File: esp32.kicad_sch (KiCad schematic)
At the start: 1 part

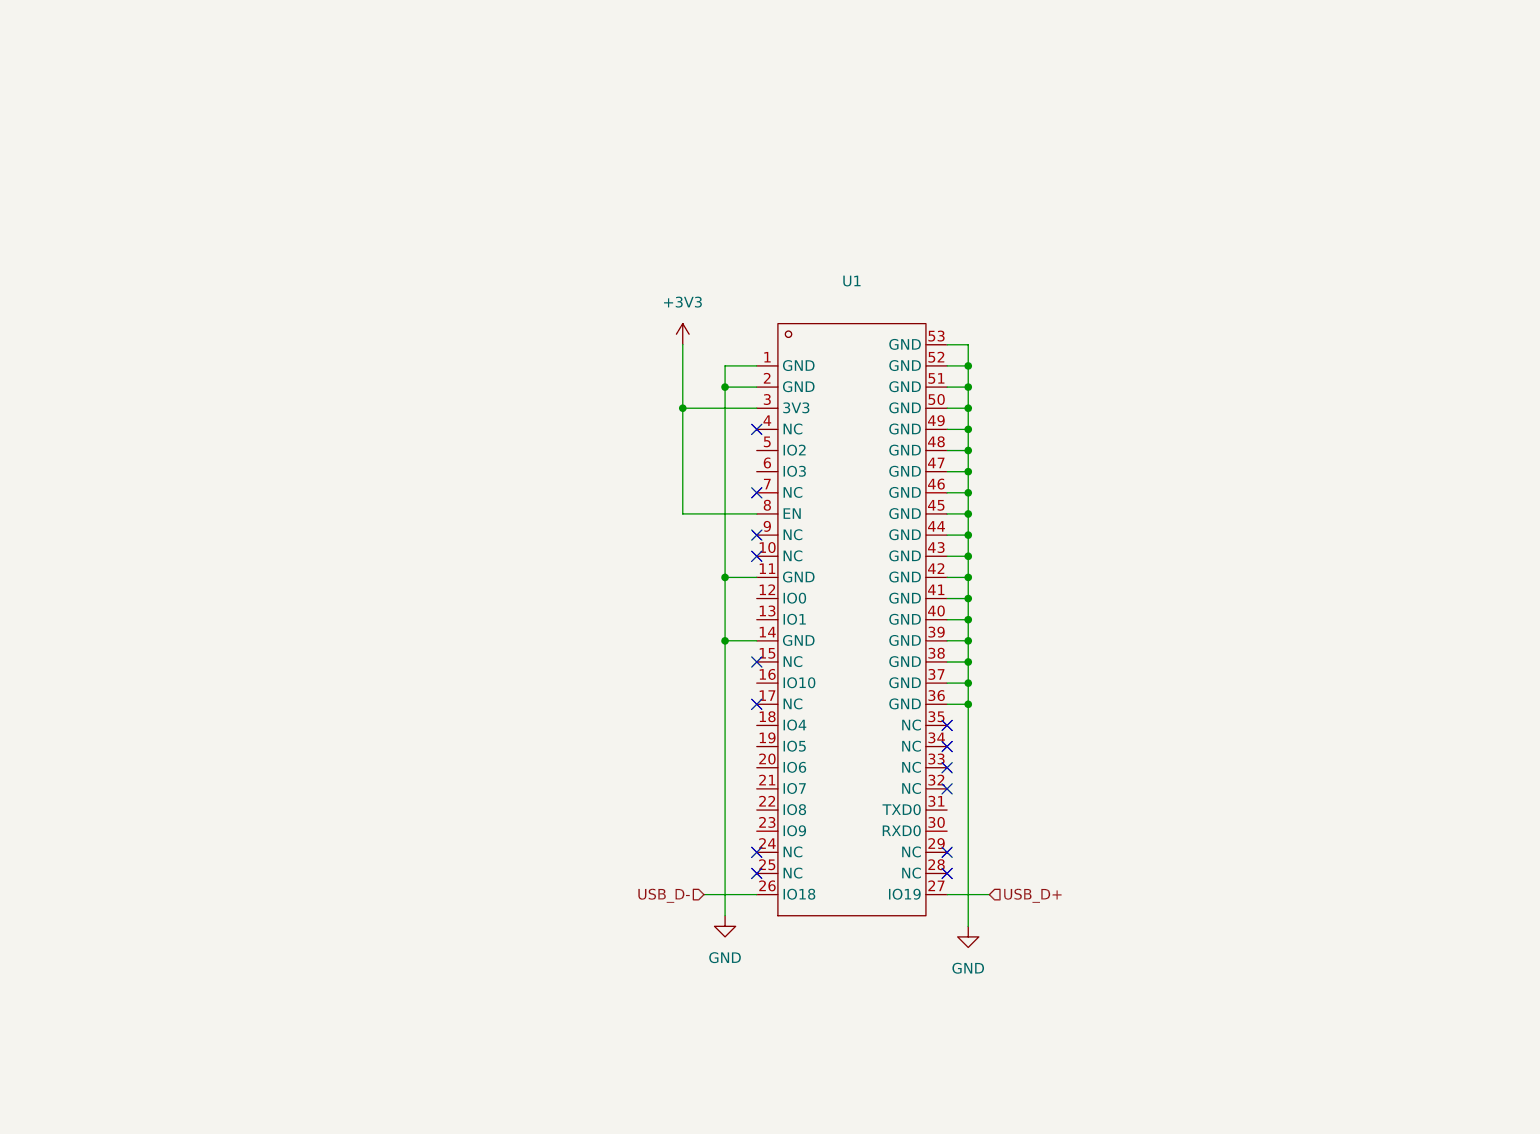
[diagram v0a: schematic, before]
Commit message: Finished the power, USB and ESP32 parts of the schematic
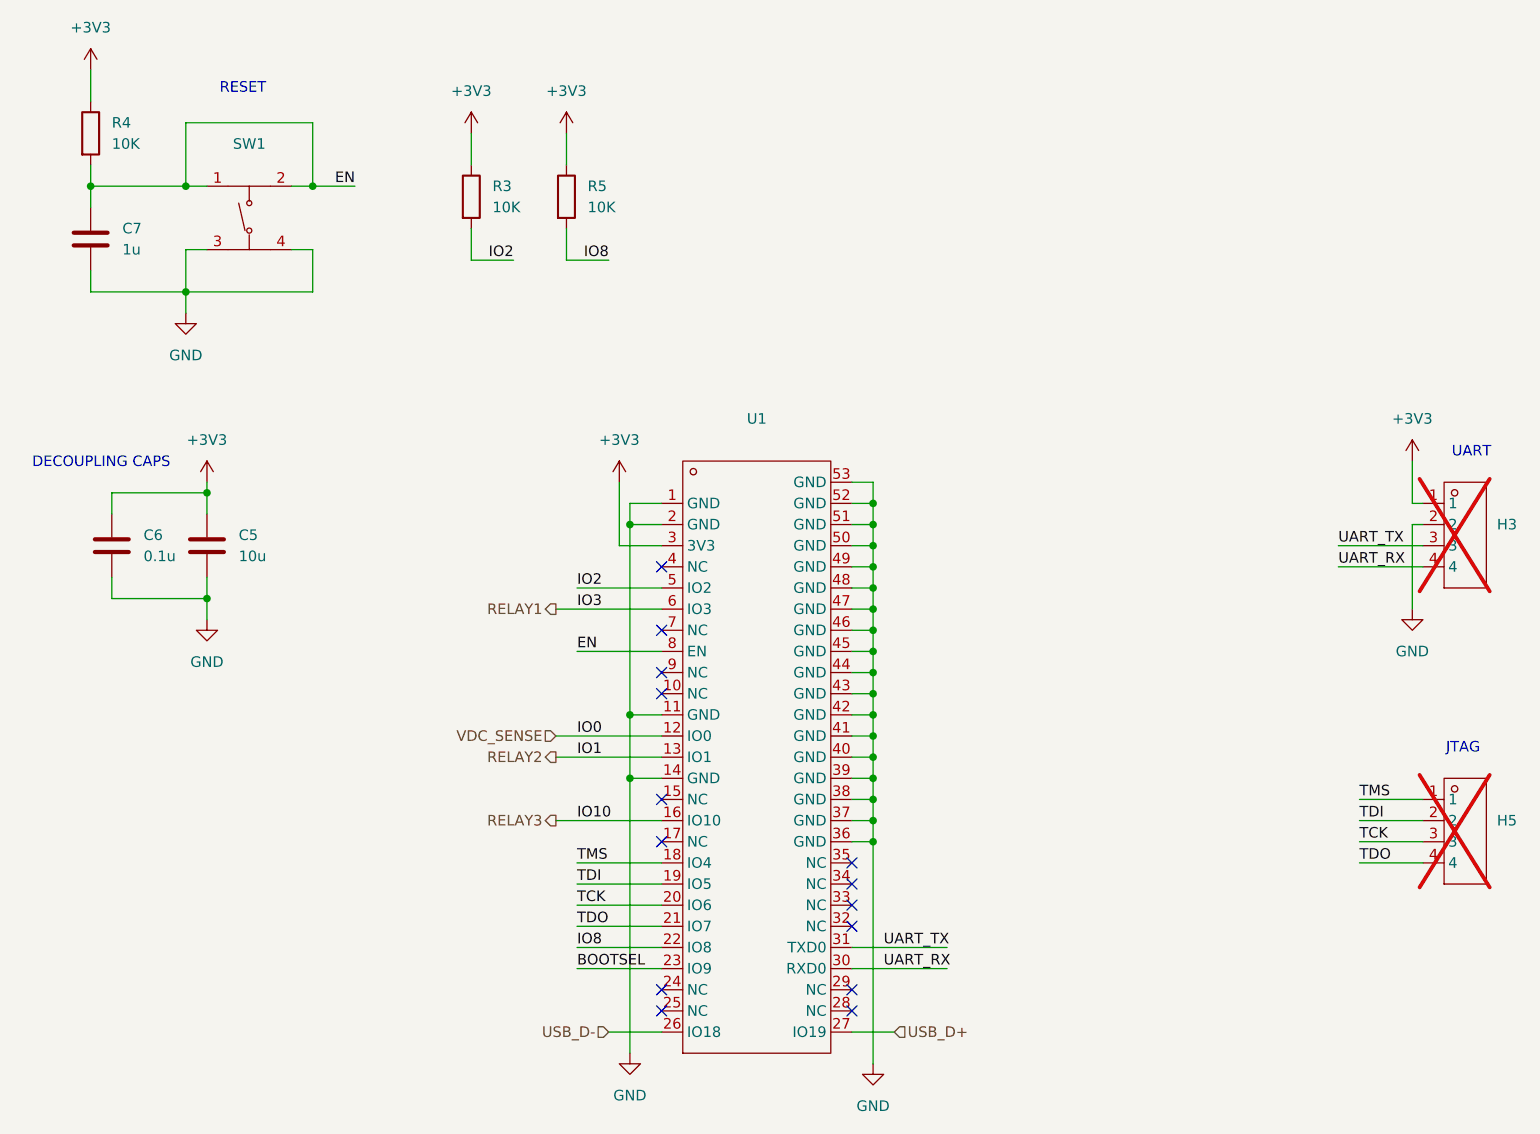
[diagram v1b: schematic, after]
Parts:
- added C5: 10u, Capacitor_SMD:C_0603_1608Metric, symbol Device:C
- added C6: 0.1u, Capacitor_SMD:C_0603_1608Metric, symbol Device:C
- added C7: 1u, Capacitor_SMD:C_0603_1608Metric, symbol Device:C
- added H3, H5: ~, EasyEDA_Lib:HDR-TH_4P-P2.54-V-M, symbol EasyEDA_Lib:PZ254V-11-04P_C2691448
- added R3, R4, R5: 10K, Resistor_SMD:R_0603_1608Metric, symbol Device:R
- added SW1: ~, EasyEDA_Lib:SW-SMD_4P-L4.2-W3.3-P2.15-LS5.1, symbol EasyEDA_Lib:TS-1089S-02526
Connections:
- net +3V3: now also C5.1, C6.1, H3.1, R3.1, R4.1, R5.1; no longer U1.8 (EN)
- net GND: now also C5.2, C6.2, C7.2, H3.2, SW1.3, SW1.4
- net VDC_SENSE: now reaches U1.12 (IO0)
- net RELAY2: now reaches U1.13 (IO1)
- net RELAY3: now reaches U1.16 (IO10)
- net TMS: now reaches U1.18 (IO4)
- net TMS: now also H5.1
- net TDI: now reaches U1.19 (IO5)
- net TDI: now also H5.2
- net TCK: now reaches U1.20 (IO6)
- net TCK: now also H5.3
- net TDO: now reaches U1.21 (IO7)
- net TDO: now also H5.4
- net IO8: now reaches U1.22 (IO8)
- net IO8: now also R5.2
- net BOOTSEL: now reaches U1.23 (IO9)
- net UART_RX: now reaches U1.30 (RXD0)
- net UART_RX: now also H3.4
- net UART_TX: now reaches U1.31 (TXD0)
- net UART_TX: now also H3.3
- net IO2: now reaches U1.5 (IO2)
- net IO2: now also R3.2
- net RELAY1: now reaches U1.6 (IO3)
- new net EN: C7.1, R4.2, SW1.1, SW1.2, U1.8 (EN)
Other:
- note added: "DECOUPLING CAPS"
- note added: "JTAG"
- note added: "RESET"
- note added: "UART"
- moved on the sheet: U1

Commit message: Finished schematics, started component placement
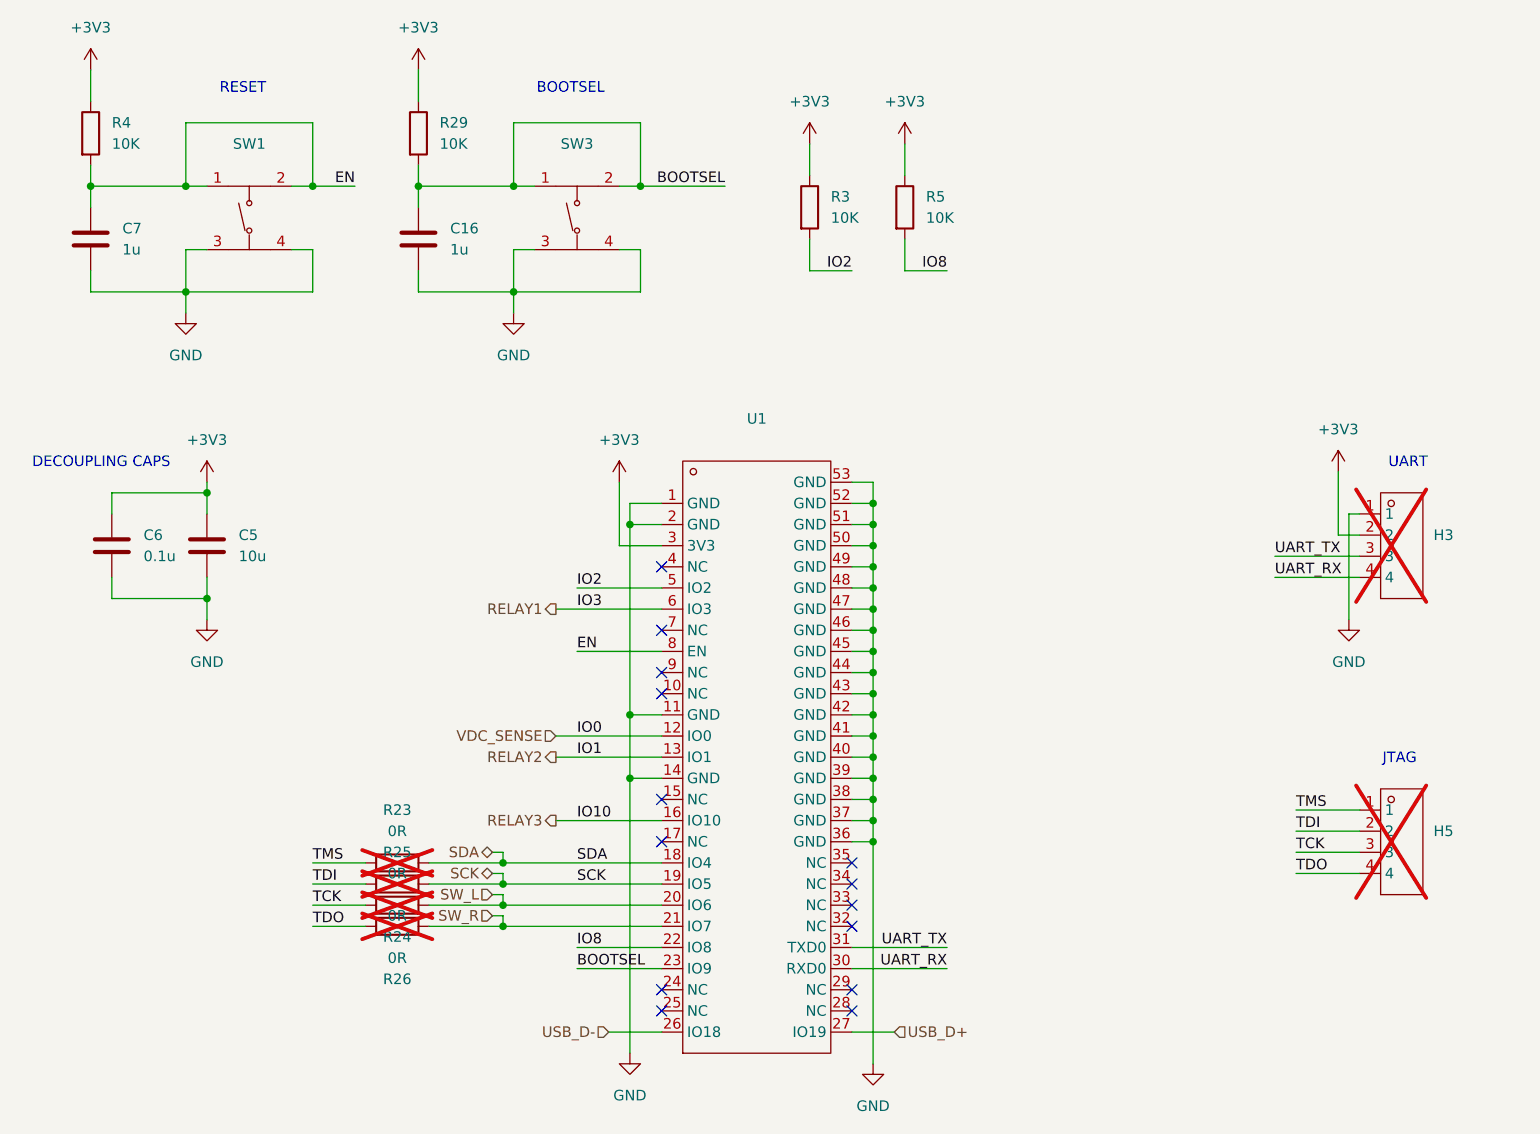
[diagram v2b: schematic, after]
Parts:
- added C16: 1u, Capacitor_SMD:C_0603_1608Metric, symbol Device:C
- added R23, R24, R25, R26: 0R, Resistor_SMD:R_0603_1608Metric, symbol Device:R
- added R29: 10K, Resistor_SMD:R_0603_1608Metric, symbol Device:R
- added SW3: ~, EasyEDA_Lib:SW-SMD_4P-L4.2-W3.3-P2.15-LS5.1, symbol EasyEDA_Lib:TS-1089S-02526
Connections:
- net +3V3: now also H3.2, R29.1; no longer H3.1
- net BOOTSEL: now also C16.1, R29.2, SW3.1, SW3.2
- net GND: now also H3.1, C16.2, SW3.3, SW3.4; no longer H3.2
- net TCK: now also R25.1; no longer U1.20 (IO6)
- net TDI: now also R24.1; no longer U1.19 (IO5)
- net TDO: now also R26.1; no longer U1.21 (IO7)
- net TMS: now also R23.1; no longer U1.18 (IO4)
- new net SCK: R24.2, U1.19 (IO5)
- new net SDA: R23.2, U1.18 (IO4)
- new net SW_L: R25.2, U1.20 (IO6)
- new net SW_R: R26.2, U1.21 (IO7)
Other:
- note added: "BOOTSEL"
- moved on the sheet: H3, H5, R3, R5
